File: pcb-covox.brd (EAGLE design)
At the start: 49 x 57 mm, 25 parts, among them X2 MJ-2135MJ-2135

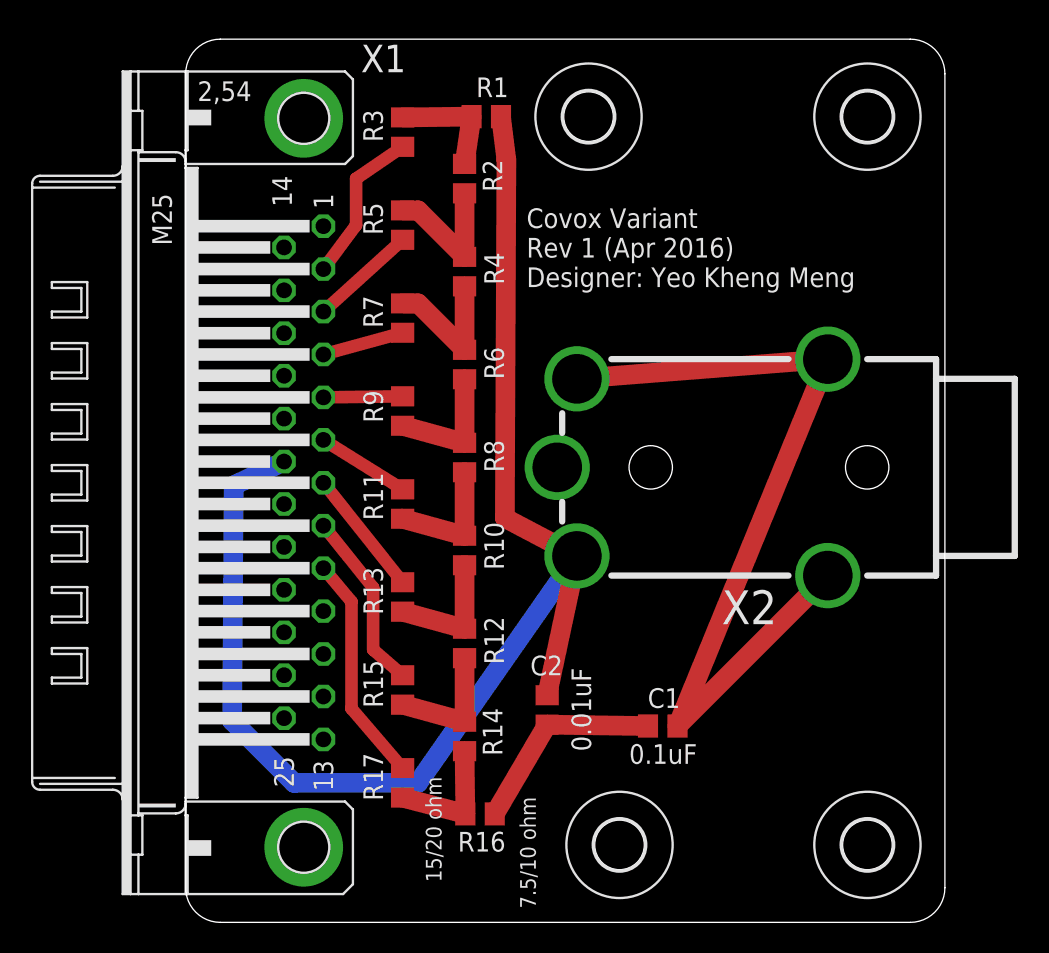
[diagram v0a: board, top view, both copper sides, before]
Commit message: corrected bug in size of audio connector
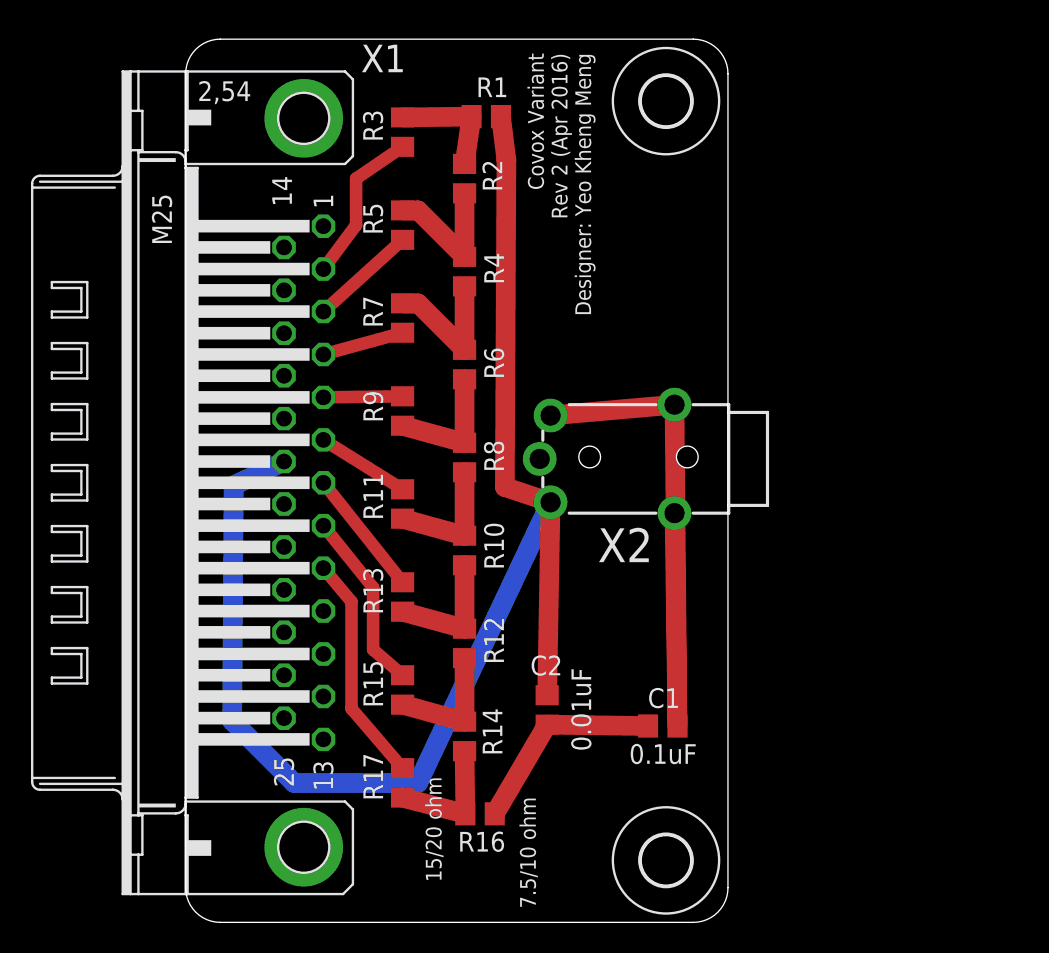
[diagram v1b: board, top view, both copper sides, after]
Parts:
- removed H3, H4: MOUNT-HOLE3.2, holes:3,2
- moved H2 48.1 mm to (31.0, 53.0)
- moved H1 13.0 mm to (31.0, 4.00)
- moved X2 8.00 mm to (29.0, 30.0)
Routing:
- net N$18: track 55.6 -> 42.5 mm
- net GND: track 90.7 -> 92.0 mm
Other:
- board size 49 x 57 mm -> 35 x 57 mm
- board text added: "Covox Variant Rev 2 (Apr 2016) Designer: Yeo Kheng Meng"
- board text removed: "Covox Variant Rev 1 (Apr 2016) Designer: Yeo Kheng Meng"
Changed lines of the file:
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@@
 <wire x1="0" y1="54.763934375" x2="0" y2="2.236065625" width="0" layer="20"/>
 <wire x1="0" y1="2.236065625" x2="2.236065625" y2="0" width="0" layer="20" curve="90"/>
-<wire x1="2.236065625" y1="0" x2="46.763934375" y2="0" width="0" layer="20"/>
-<wire x1="46.763934375" y1="0" x2="49" y2="2.236065625" width="0" layer="20" curve="90"/>
-<wire x1="49" y1="2.236065625" x2="49" y2="54.763934375" width="0" layer="20"/>
-<wire x1="49" y1="54.763934375" x2="46.763934375" y2="57" width="0" layer="20" curve="90"/>
-<wire x1="46.763934375" y1="57" x2="2.236065625" y2="57" width="0" layer="20"/>
+<wire x1="2.236065625" y1="0" x2="32.763934375" y2="0" width="0" layer="20"/>
+<wire x1="32.763934375" y1="0" x2="35" y2="2.236065625" width="0" layer="20" curve="90"/>
+<wire x1="35" y1="2.236065625" x2="35" y2="54.763934375" width="0" layer="20"/>
+<wire x1="35" y1="54.763934375" x2="32.763934375" y2="57" width="0" layer="20" curve="90"/>
+<wire x1="32.763934375" y1="57" x2="2.236065625" y2="57" width="0" layer="20"/>
 <wire x1="2.236065625" y1="57" x2="0" y2="54.763934375" width="0" layer="20" curve="90"/>
 <text x="15.5" y="9.4" size="1.016" layer="21" rot="R270">15/20 ohm</text>
 <text x="22.6" y="0.9" size="1.016" layer="21" rot="R90">7.5/10 ohm</text>
-<text x="22" y="41" size="1.27" layer="21">Covox Variant
-Rev 1 (Apr 2016)
+<text x="22.1" y="56.1" size="1.016" layer="21" rot="R270">Covox Variant
+Rev 2 (Apr 2016)
 Designer: Yeo Kheng Meng</text>
 </plain>
@@
 <attribute name="VALUE" x="11.46" y="9.635" size="1.27" layer="27" rot="R270"/>
 </element>
-<element name="X2" library="mj-2135" package="MJ-2135" value="MJ-2135MJ-2135" x="37" y="30" smashed="yes" rot="R270">
-<attribute name="NAME" x="38.16" y="21.43" size="2.1844" layer="25" rot="R180"/>
-</element>
-<element name="H1" library="holes" package="3,2" value="MOUNT-HOLE3.2" x="44" y="5"/>
-<element name="H2" library="holes" package="3,2" value="MOUNT-HOLE3.2" x="28" y="5"/>
-<element name="H3" library="holes" package="3,2" value="MOUNT-HOLE3.2" x="44" y="52"/>
-<element name="H4" library="holes" package="3,2" value="MOUNT-HOLE3.2" x="26" y="52"/>
+<element name="X2" library="mj-2135" package="MJ-2135" value="MJ-2135MJ-2135" x="29" y="30" smashed="yes" rot="R270">
+<attribute name="NAME" x="30.16" y="25.43" size="2.1844" layer="25" rot="R180"/>
+</element>
+<element name="H1" library="holes" package="3,2" value="MOUNT-HOLE3.2" x="31" y="4"/>
+<element name="H2" library="holes" package="3,2" value="MOUNT-HOLE3.2" x="31" y="53"/>
 </elements>
 <signals>
@@
 <wire x1="3" y1="13" x2="7" y2="9" width="1.27" layer="16"/>
 <wire x1="7" y1="9" x2="15" y2="9" width="1.27" layer="16"/>
-<wire x1="15" y1="9" x2="25.2525" y2="23.65" width="1.27" layer="16"/>
+<wire x1="15" y1="9" x2="23.55" y2="27.11" width="1.27" layer="16"/>
 <wire x1="20.35" y1="52" x2="20.7" y2="49.2" width="1.27" layer="1"/>
-<wire x1="20.7" y1="49.2" x2="20.6" y2="26.1" width="1.27" layer="1"/>
-<wire x1="20.6" y1="26.1" x2="25.2525" y2="23.65" width="1.27" layer="1"/>
-<wire x1="23.33" y1="14.66" x2="25.2525" y2="23.65" width="1.27" layer="1"/>
+<wire x1="20.7" y1="49.2" x2="20.6" y2="28.1" width="1.27" layer="1"/>
+<wire x1="20.6" y1="28.1" x2="23.55" y2="27.11" width="1.27" layer="1"/>
+<wire x1="23.33" y1="14.66" x2="23.55" y2="27.11" width="1.27" layer="1"/>
 </signal>
 <signal name="N$1">
@@
 <contactref element="X2" pad="P$4"/>
 <contactref element="X2" pad="P$3"/>
-<wire x1="31.74" y1="12.67" x2="41.445" y2="22.38" width="1.27" layer="1"/>
-<wire x1="41.445" y1="36.35" x2="31.74" y2="12.67" width="1.27" layer="1"/>
-<wire x1="41.445" y1="36.35" x2="25.2525" y2="35.08" width="1.27" layer="1"/>
+<wire x1="31.74" y1="12.67" x2="31.55" y2="26.41" width="1.27" layer="1"/>
+<wire x1="31.55" y1="33.41" x2="31.74" y2="12.67" width="1.27" layer="1"/>
+<wire x1="31.55" y1="33.41" x2="23.55" y2="32.71" width="1.27" layer="1"/>
 </signal>
 </signals>

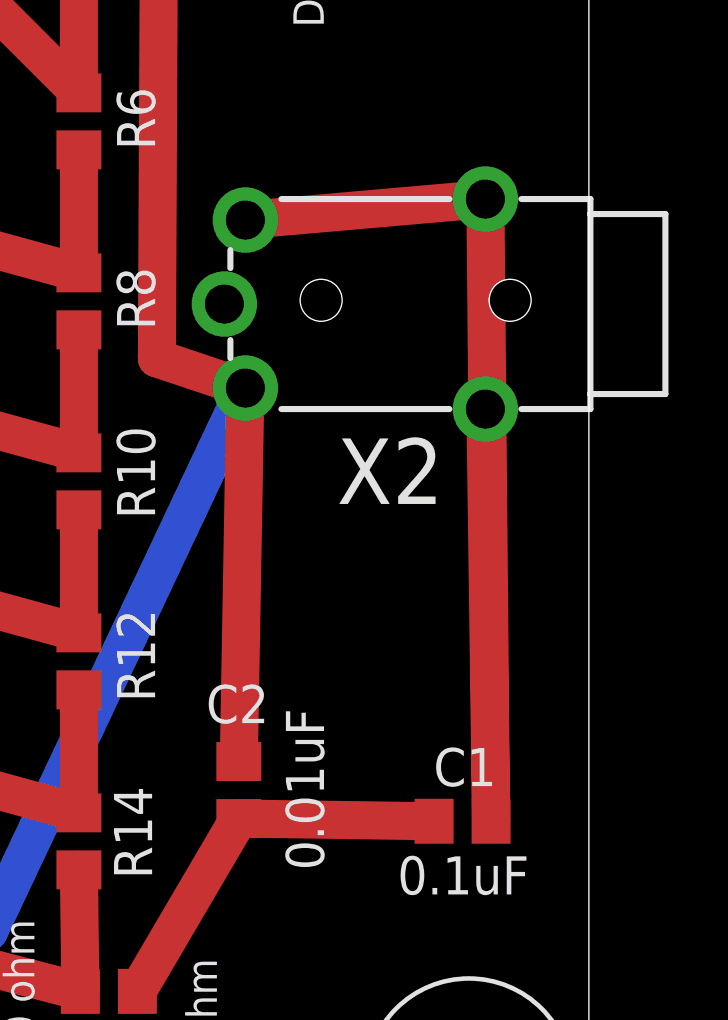
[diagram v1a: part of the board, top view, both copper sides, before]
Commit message: correct drc error
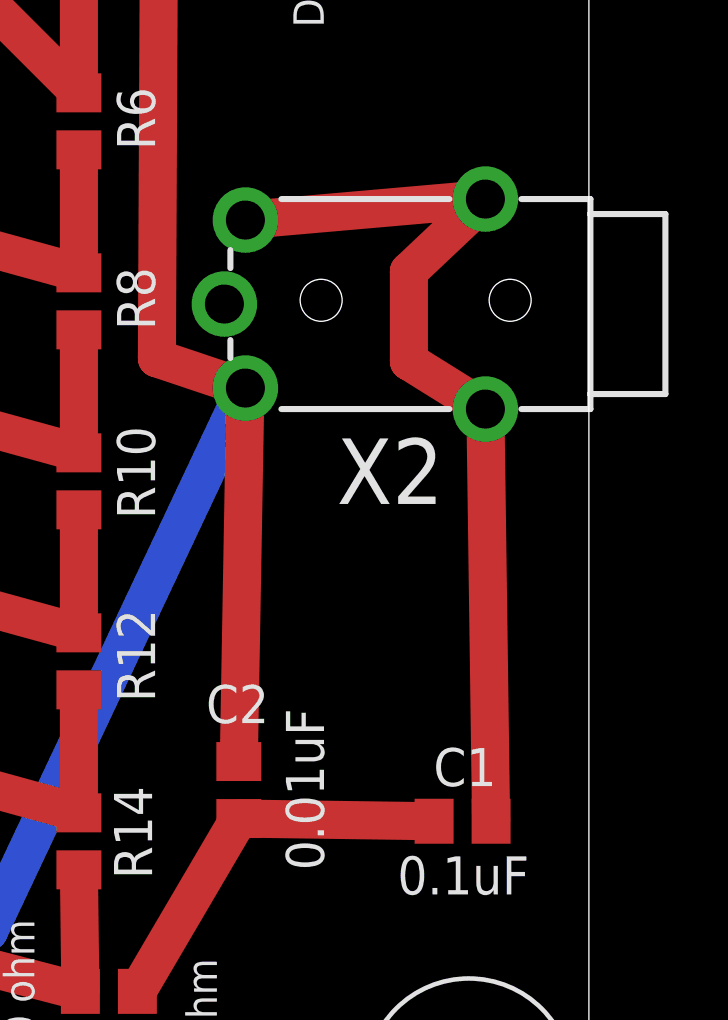
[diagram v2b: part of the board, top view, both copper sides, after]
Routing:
- net N$18: track 42.5 -> 31.3 mm
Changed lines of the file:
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@@
 <contactref element="X2" pad="P$3"/>
 <wire x1="31.74" y1="12.67" x2="31.55" y2="26.41" width="1.27" layer="1"/>
-<wire x1="31.55" y1="33.41" x2="31.74" y2="12.67" width="1.27" layer="1"/>
 <wire x1="31.55" y1="33.41" x2="23.55" y2="32.71" width="1.27" layer="1"/>
+<wire x1="31.55" y1="26.41" x2="29" y2="28" width="1.27" layer="1"/>
+<wire x1="29" y1="28" x2="29" y2="31" width="1.27" layer="1"/>
+<wire x1="29" y1="31" x2="31.55" y2="33.41" width="1.27" layer="1"/>
 </signal>
 </signals>
